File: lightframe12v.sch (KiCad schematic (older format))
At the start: 52 parts, among them J1 PJ-077, J2 Conn_01x08_Female, J3 Conn_01x08_Female, J4 Conn_01x06_Female, Q1 MMBT2222, Q2 MMBT2222, SW1 SW_Push, SW2 SW_Push, U1 TPS563207s, U2 TLC6C598PWR, U3 ESP32-WROOM-32U, U4 TLC6C598PWR

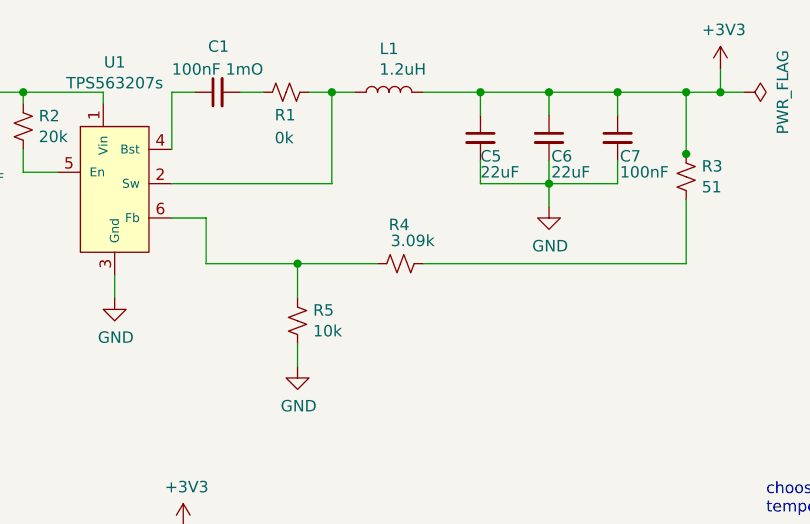
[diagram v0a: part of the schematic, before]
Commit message: Adds fiducials.
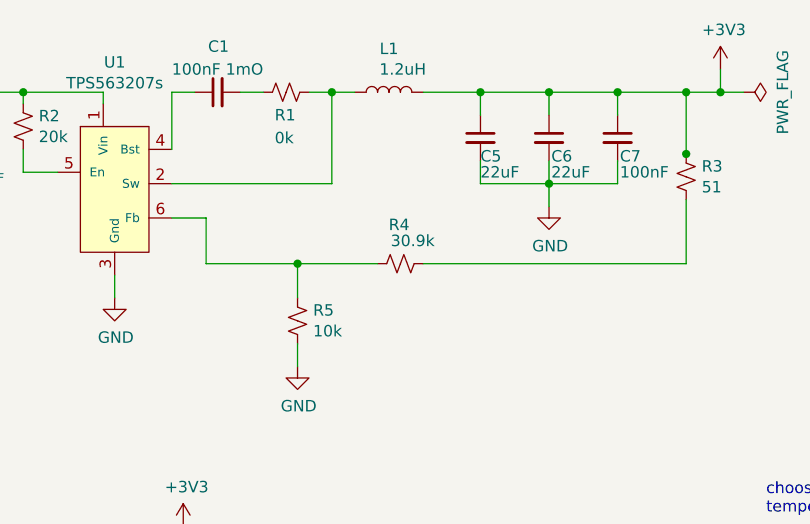
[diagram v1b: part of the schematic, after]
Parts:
- R4: value 3.09k -> 30.9k
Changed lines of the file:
@@
 P 6050 1600
 F 0 "R4" V 6220 1560 50  0000 L CNN
-F 1 "3.09k" V 6150 1450 50  0000 L CNN
+F 1 "30.9k" V 6150 1450 50  0000 L CNN
 F 2 "digikey-footprints:0603" H 6050 1600 50  0001 C CNN
 F 3 "~" H 6050 1600 50  0001 C CNN

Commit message: Updates header footprints.
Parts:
- J2, J3: footprint keith:Pinheader1x8 2.54_Drill1.02mm -> Connector_PinHeader_2.54mm:PinHeader_1x08_P2.54mm_Vertical
- J4: footprint keith:Pinheader1x6 2.54_Drill1.02mm -> Connector_PinHeader_2.54mm:PinHeader_1x06_P2.54mm_Vertical
- e1: footprint keith:Pinheader1x10 2.54_Drill1.02mm -> Connector_PinHeader_2.54mm:PinHeader_1x10_P2.54mm_Vertical
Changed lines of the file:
@@
 F 0 "J3" H 10328 1426 50  0000 L CNN
 F 1 "Conn_01x08_Female" H 10328 1335 50  0000 L CNN
-F 2 "keith:Pinheader1x8 2.54_Drill1.02mm" H 10300 1450 50  0001 C CNN
+F 2 "Connector_PinHeader_2.54mm:PinHeader_1x08_P2.54mm_Vertical" H 10300 1450 50  0001 C CNN
 F 3 "~" H 10300 1450 50  0001 C CNN
 	1    10300 1450
@@
 F 0 "J4" H 10328 2226 50  0000 L CNN
 F 1 "Conn_01x06_Female" H 10328 2135 50  0000 L CNN
-F 2 "keith:Pinheader1x6 2.54_Drill1.02mm" H 10300 2250 50  0001 C CNN
+F 2 "Connector_PinHeader_2.54mm:PinHeader_1x06_P2.54mm_Vertical" H 10300 2250 50  0001 C CNN
 F 3 "~" H 10300 2250 50  0001 C CNN
 	1    10300 2250
@@
 F 0 "e1" H 10328 3276 50  0000 L CNN
 F 1 "Conn_01x10_Female" H 10328 3185 50  0000 L CNN
-F 2 "keith:Pinheader1x10 2.54_Drill1.02mm" H 10300 3250 50  0001 C CNN
+F 2 "Connector_PinHeader_2.54mm:PinHeader_1x10_P2.54mm_Vertical" H 10300 3250 50  0001 C CNN
 F 3 "~" H 10300 3250 50  0001 C CNN
 	1    10300 3250
@@
 F 0 "J2" H 8978 1426 50  0000 L CNN
 F 1 "Conn_01x08_Female" H 8978 1335 50  0000 L CNN
-F 2 "keith:Pinheader1x8 2.54_Drill1.02mm" H 8950 1450 50  0001 C CNN
+F 2 "Connector_PinHeader_2.54mm:PinHeader_1x08_P2.54mm_Vertical" H 8950 1450 50  0001 C CNN
 F 3 "~" H 8950 1450 50  0001 C CNN
 	1    8950 1450

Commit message: changes footprint to TLC5971
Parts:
- U2, U4: footprint keith:TLC6C598 -> Package_SO:HTSSOP-20-1EP_4.4x6.5mm_P0.65mm_EP3.4x6.5mm_Mask2.75x3.43mm_ThermalVias
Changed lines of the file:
@@
 F 0 "U2" H 6350 4381 50  0000 C CNN
 F 1 "TLC6C598PWR" H 6350 4290 50  0000 C CNN
-F 2 "keith:TLC6C598" H 6350 3700 50  0001 C CNN
+F 2 "Package_SO:HTSSOP-20-1EP_4.4x6.5mm_P0.65mm_EP3.4x6.5mm_Mask2.75x3.43mm_ThermalVias" H 6350 3700 50  0001 C CNN
 F 3 "" H 6350 3700 50  0001 C CNN
 	1    6350 3700
@@
 F 0 "U4" H 6800 6531 50  0000 C CNN
 F 1 "TLC6C598PWR" H 6800 6440 50  0000 C CNN
-F 2 "keith:TLC6C598" H 6800 5850 50  0001 C CNN
+F 2 "Package_SO:HTSSOP-20-1EP_4.4x6.5mm_P0.65mm_EP3.4x6.5mm_Mask2.75x3.43mm_ThermalVias" H 6800 5850 50  0001 C CNN
 F 3 "" H 6800 5850 50  0001 C CNN
 	1    6800 5850

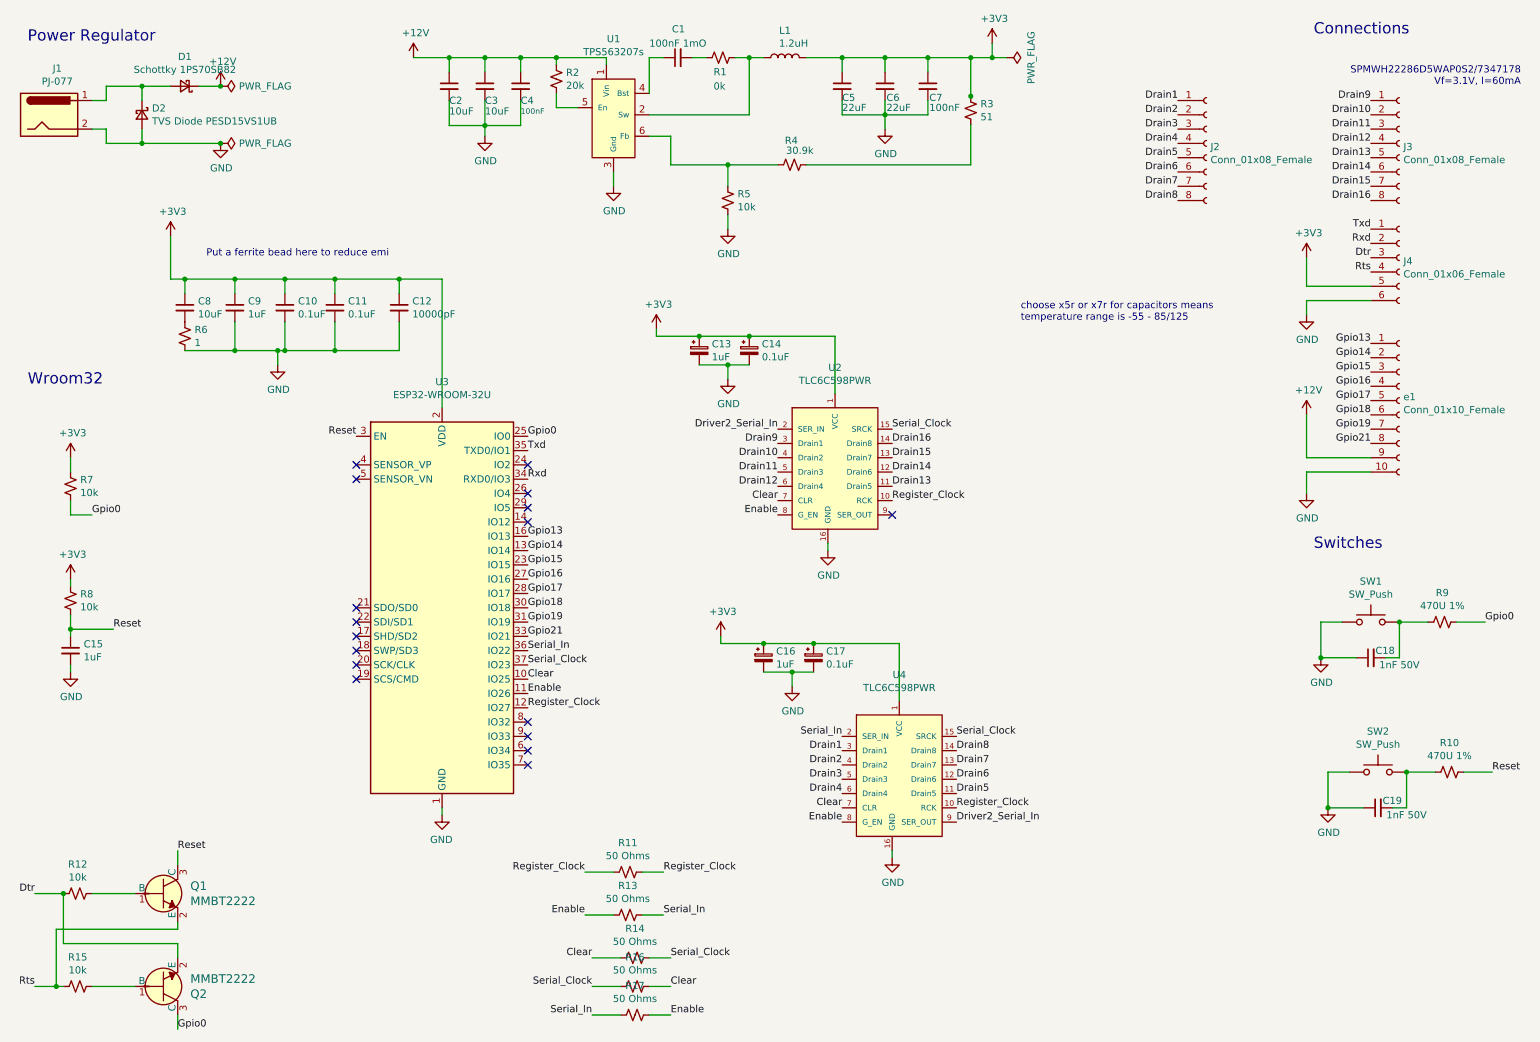
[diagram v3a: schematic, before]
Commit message: creates new symbol TLC5971
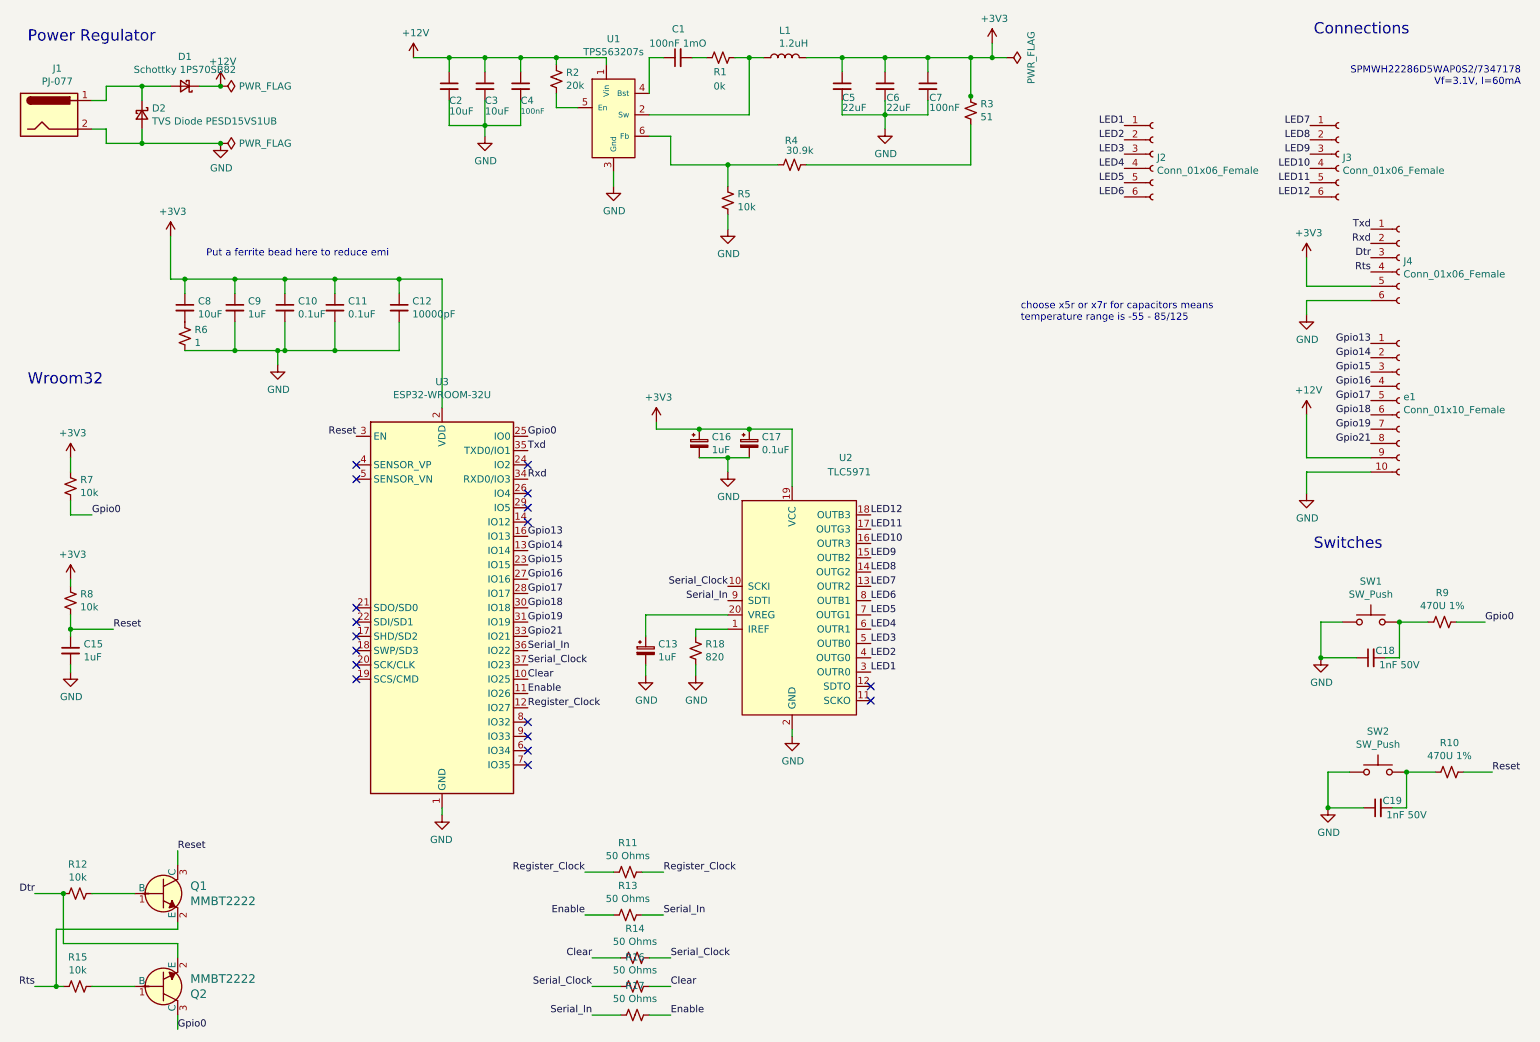
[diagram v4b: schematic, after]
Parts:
- removed C14: 0.1uF, digikey-footprints:0603, symbol Device:CP_Small
- removed J2, J3: Conn_01x08_Female, Connector_PinHeader_2.54mm:PinHeader_1x08_P2.54mm_Vertical, symbol Connector:Conn_01x08_Female
- removed U2, U4: TLC6C598PWR, Package_SO:HTSSOP-20-1EP_4.4x6.5mm_P0.65mm_EP3.4x6.5mm_Mask2.75x3.43mm_ThermalVias, symbol lightframe12v-rescue:TLC6C598PWR-keith-lightframe12v-rescue
- added J2, J3: Conn_01x06_Female, Connector_PinSocket_2.54mm:PinSocket_1x06_P2.54mm_Vertical, symbol Connector:Conn_01x06_Female
- added R18: 820, digikey-footprints:0603, symbol Device:R_Small_US
- added U2: TLC5971, Package_SO:HTSSOP-20-1EP_4.4x6.5mm_P0.65mm_EP3.4x6.5mm_Mask2.75x3.43mm_ThermalVias, symbol lightframe:TLC5971
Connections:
- net +3V3: now also U2.19 (VCC); no longer C13.1
- net GND: now also R18.2, U2.2 (GND)
- net Serial_Clock: now also U2.10 (SCKI)
- net Serial_In: now also U2.9 (SDTI)
- new net: R18.1, U2.1 (IREF)
- new net: C13.1, U2.20 (VREG)
- new net LED1: J2.1 (Pin_1), U2.3 (OUTR0)
- new net LED10: J3.4 (Pin_4), U2.16 (OUTR3)
- new net LED11: J3.5 (Pin_5), U2.17 (OUTG3)
- new net LED12: J3.6 (Pin_6), U2.18 (OUTB3)
- new net LED2: J2.2 (Pin_2), U2.4 (OUTG0)
- new net LED3: J2.3 (Pin_3), U2.5 (OUTB0)
- new net LED4: J2.4 (Pin_4), U2.6 (OUTR1)
- new net LED5: J2.5 (Pin_5), U2.7 (OUTG1)
- new net LED6: J2.6 (Pin_6), U2.8 (OUTB1)
- new net LED7: J3.1 (Pin_1), U2.13 (OUTR2)
- new net LED8: J3.2 (Pin_2), U2.14 (OUTG2)
- new net LED9: J3.3 (Pin_3), U2.15 (OUTB2)
- no-connect marks 17 -> 18
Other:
- moved on the sheet: C16, C17

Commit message: initial layout of wroom
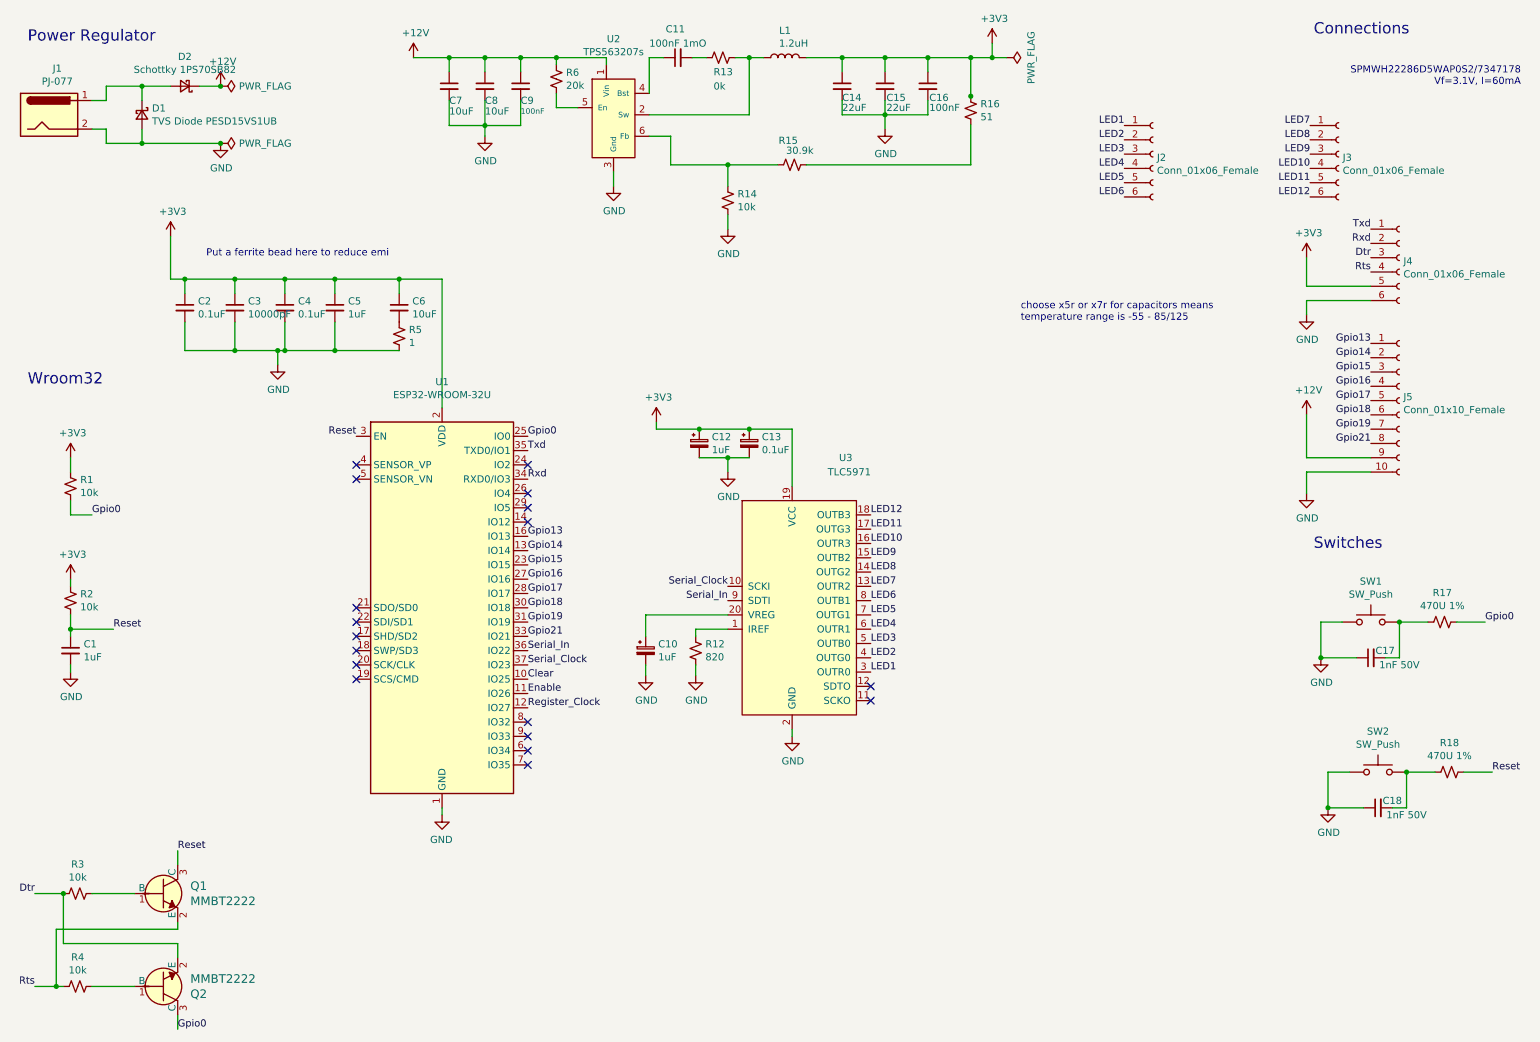
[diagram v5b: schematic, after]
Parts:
- removed R11, R13, R14, R16, R17: 50 Ohms, Resistor_SMD:R_0402_1005Metric, symbol Device:R_Small_US
- renumbered C15 to C1, C13 to C10, C1 to C11, C16 to C12, C17 to C13, C5 to C14, C6 to C15, C7 to C16, C18 to C17, C19 to C18, C11 to C2, C12 to C3, C10 to C4, C9 to C5, C8 to C6, C2 to C7, C3 to C8, C4 to C9, D2 to D1, D1 to D2, e1 to J5, R7 to R1, R18 to R12, R1 to R13, R5 to R14, R4 to R15, R3 to R16, R9 to R17, R10 to R18, R8 to R2, R12 to R3, R15 to R4, R6 to R5, R2 to R6, U3 to U1, U1 to U2, U2 to U3
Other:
- moved on the sheet: C2, C3, C5, C6, R5
